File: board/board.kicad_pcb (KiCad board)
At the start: 2 copper layers, 45 x 94 mm, 13 parts, among them J1 020_1000BASE-T_with_CT, J2 003_power, J3 008_USB, J4 001_I2C, J5 008_USB, J6 002_SPI, J7 010_UART, U1 VAR-SOM

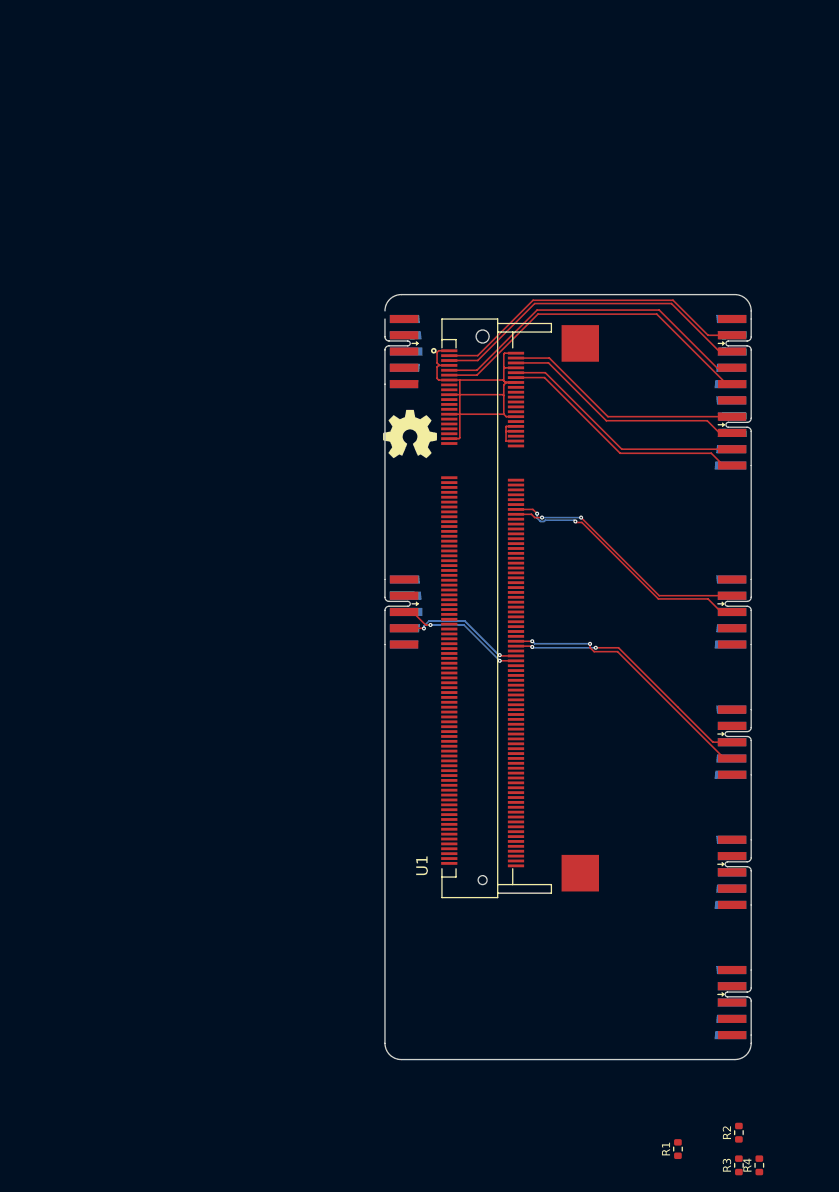
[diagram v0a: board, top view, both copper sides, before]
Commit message: added RGMII interface
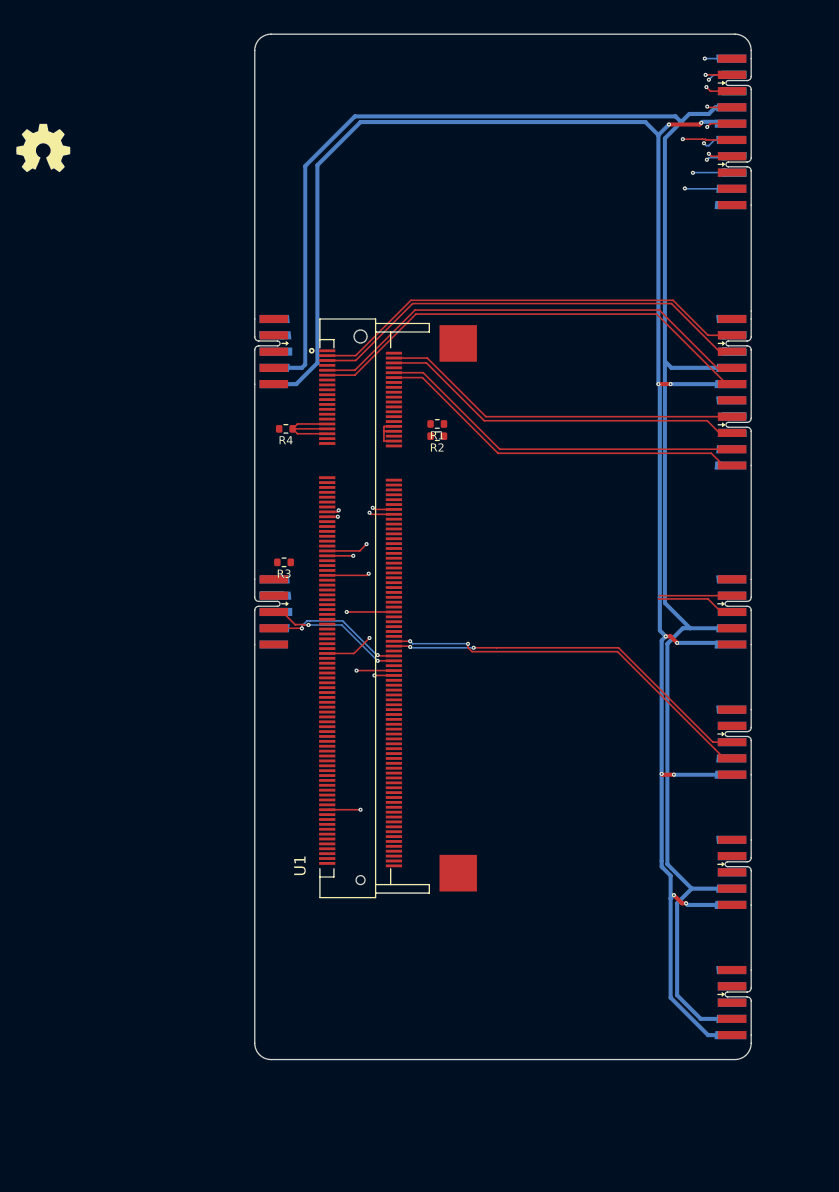
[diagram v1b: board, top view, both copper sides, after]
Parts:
- added J8: 015_RGMII, on_edge:on_edge_2x10_host, F.Cu at (174.0, 24.0)
- moved R4 107.6 mm to (116.8, 65.5), turned to 180 degrees
- moved R1 93.9 mm to (135.4, 64.9), turned to 180 degrees
- moved R2 93.3 mm to (135.4, 66.4), turned to 180 degrees
- moved R3 92.8 mm to (116.6, 81.9), turned to 180 degrees
- moved LOGO1 57.2 mm to (87.0, 31.0)
- moved J2 16.0 mm to (113.0, 56.0)
- moved J3 16.0 mm to (113.0, 88.0)
- moved U1 15.0 mm to (126.0, 87.5)
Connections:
- J1 pad 1: unconnected-(J1-Pad1) -> GND
- J1 pad 11: unconnected-(J1-Pad11) -> GND
- J3 pad 10: unconnected-(J3-Pad10) -> +5V
- J5 pad 10: unconnected-(J5-Pad10) -> +5V
- R1 pad 1: /var-som/VCC -> +3.3V
- R2 pad 1: /var-som/VCC -> +3.3V
- R3 pad 2: /var-som/VCC -> +3.3V
- R4 pad 2: /var-som/VCC -> +3.3V
- U1 pad 103: /var-som/VCC -> +3.3V
- U1 pad 105: /var-som/VCC -> +3.3V
- U1 pad 107: /var-som/VCC -> +3.3V
- U1 pad 109: /var-som/VCC -> +3.3V
- U1 pad 111: /var-som/VCC -> +3.3V
- U1 pad 113: unconnected-(U1-Pad113) -> /var-som/ENET1_TX_CTL
- U1 pad 120: unconnected-(U1-Pad120) -> /var-som/ENET1_RX_CTL
- U1 pad 122: unconnected-(U1-Pad122) -> /var-som/ENET1_RXD0
- U1 pad 177: unconnected-(U1-Pad177) -> /var-som/ENET1_TXD1
- U1 pad 32: /var-som/VCC -> +3.3V
- U1 pad 34: /var-som/VCC -> +3.3V
- U1 pad 38: /var-som/VCC -> +3.3V
- U1 pad 52: unconnected-(U1-Pad52) -> /UART5_TX
- U1 pad 53: unconnected-(U1-Pad53) -> /UART5_RX
- U1 pad 54: /UART5_RX -> /var-som/ENET1_RXD3
- U1 pad 55: unconnected-(U1-Pad55) -> /var-som/ENET1_TXD3
- U1 pad 56: /UART5_TX -> /var-som/ENET1_TXD2
- U1 pad 57: unconnected-(U1-Pad57) -> /var-som/ENET1_RXC
- U1 pad 71: unconnected-(U1-Pad71) -> /var-som/ENET1_RXD2
- U1 pad 73: unconnected-(U1-Pad73) -> /var-som/ENET1_TXD0
- U1 pad 81: unconnected-(U1-Pad81) -> /var-som/ENET1_RXD1
- U1 pad 96: unconnected-(U1-Pad96) -> /var-som/ENET1_TXC
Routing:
- net +5V: track 0.00 -> 235.5 mm, vias 0 -> 10
- net +3.3V: track 0.00 -> 229.3 mm
- net /var-som/ENET1_TXD1: track 0.00 -> 116.9 mm, vias 0 -> 2
- net /var-som/ENET1_RX_CTL: track 0.00 -> 104.3 mm, vias 0 -> 2
- net /var-som/ENET1_TXC: track 0.00 -> 98.3 mm, vias 0 -> 2
- net /var-som/ENET1_RXD0: track 0.00 -> 95.1 mm, vias 0 -> 2
- net /var-som/ENET1_TX_CTL: track 0.00 -> 92.2 mm, vias 0 -> 2
- net /var-som/ENET1_TXD0: track 0.00 -> 87.3 mm, vias 0 -> 2
- net /var-som/ENET1_RXC: track 0.00 -> 84.6 mm, vias 0 -> 2
- net /var-som/ENET1_RXD1: track 0.00 -> 82.9 mm, vias 0 -> 2
- net /var-som/ENET1_RXD2: track 0.00 -> 77.8 mm, vias 0 -> 2
- net /var-som/ENET1_TXD2: track 0.00 -> 76.9 mm, vias 0 -> 2
- net /var-som/ENET1_TXD3: track 0.00 -> 75.1 mm, vias 0 -> 2
- net /var-som/ENET1_RXD3: track 0.00 -> 68.9 mm, vias 0 -> 2
- net GND: track 51.3 -> 0.00 mm
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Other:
- board size 45 x 94 mm -> 61 x 126 mm
- copper layers 2 -> 4

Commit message: added uSD card
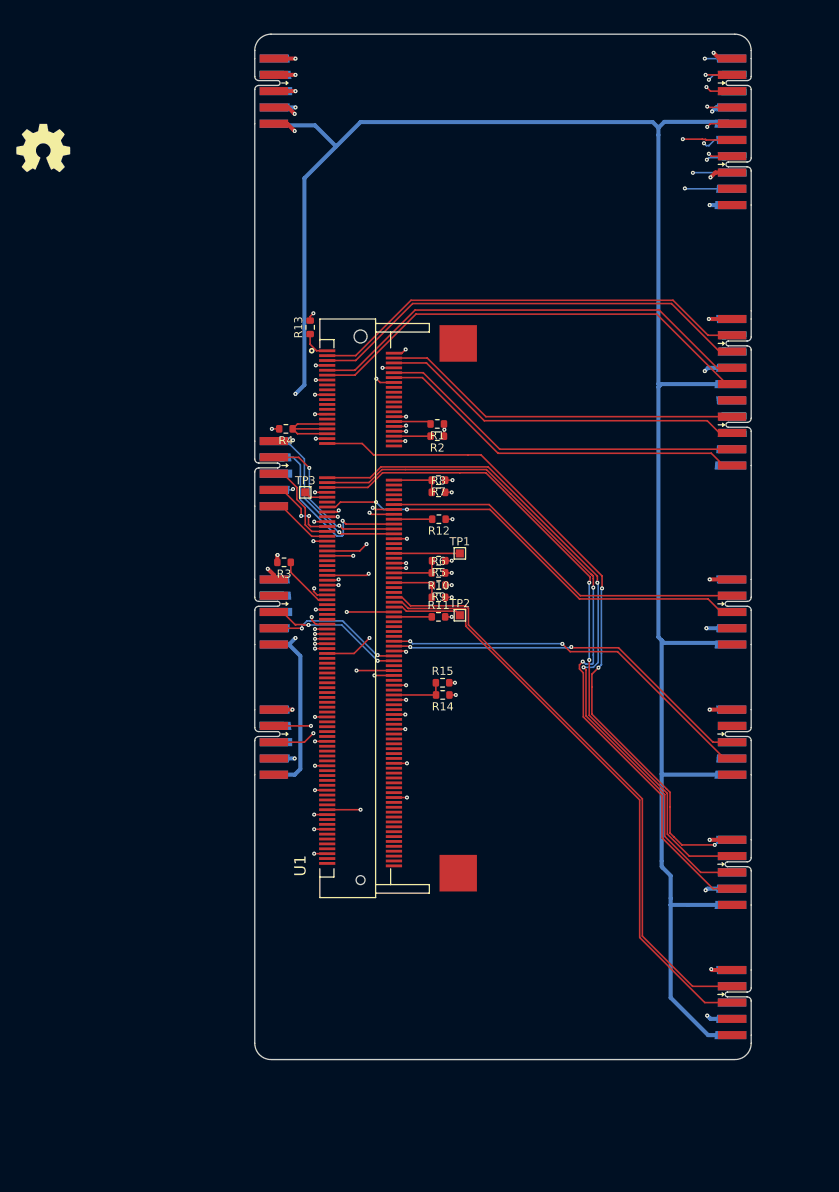
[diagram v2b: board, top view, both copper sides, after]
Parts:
- added J10: 018_QSPI, on_edge:on_edge_2x05_device, F.Cu at (113.0, 71.0)
- added J9: 010_UART, on_edge:on_edge_2x05_device, F.Cu at (113.0, 104.0)
- added R10: 560R, Resistor_SMD:R_0603_1608Metric, F.Cu at (135.6, 86.2)
- added R11: 560R, Resistor_SMD:R_0603_1608Metric, F.Cu at (135.6, 88.6)
- added R12: 0R, Resistor_SMD:R_0603_1608Metric, F.Cu at (135.6, 76.6)
- added R13: 0R, Resistor_SMD:R_0603_1608Metric, F.Cu at (119.8, 53.0)
- added R14: 0R, Resistor_SMD:R_0603_1608Metric, F.Cu at (136.1, 98.2)
- added R15: 560R, Resistor_SMD:R_0603_1608Metric, F.Cu at (136.1, 96.7)
- added R5: 560R, Resistor_SMD:R_0603_1608Metric, F.Cu at (135.6, 81.7)
- added R6: 560R, Resistor_SMD:R_0603_1608Metric, F.Cu at (135.6, 83.2)
- added R7: 560R, Resistor_SMD:R_0603_1608Metric, F.Cu at (135.6, 71.8)
- added R8: 560R, Resistor_SMD:R_0603_1608Metric, F.Cu at (135.6, 73.3)
- added R9: 0R, Resistor_SMD:R_0603_1608Metric, F.Cu at (135.6, 84.7)
- added TP1: USB_B_VBUS_ID1, TestPoint:TestPoint_Pad_1.0x1.0mm, F.Cu at (138.2, 80.8)
- added TP2: USB_B_VBUS_ID2, TestPoint:TestPoint_Pad_1.0x1.0mm, F.Cu at (138.2, 88.4)
- added TP3: base_peripherals_power, TestPoint:TestPoint_Pad_1.0x1.0mm, F.Cu at (119.2, 73.3)
- moved J2 32.0 mm to (113.0, 24.0)
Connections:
- J4 pad 2: unconnected-(J4-Pad2) -> /var-som/I2C3_SDA
- J4 pad 3: unconnected-(J4-Pad3) -> /var-som/I2C3_SCL
- J6 pad 2: unconnected-(J6-Pad2) -> /var-som/SPI4_MOSI
- J6 pad 3: unconnected-(J6-Pad3) -> /var-som/SPI4_MISO
- J6 pad 4: unconnected-(J6-Pad4) -> /var-som/SPI4_SCLK
- J6 pad 6: unconnected-(J6-Pad6) -> /var-som/SPI4_SS
- U1 pad 1: GND -> Net-(U1-Pad1)
- U1 pad 130: unconnected-(U1-Pad130) -> Net-(U1-Pad130)
- U1 pad 178: unconnected-(U1-Pad178) -> GND
- U1 pad 39: unconnected-(U1-Pad39) -> /var-som/SPI4_SS
- U1 pad 41: unconnected-(U1-Pad41) -> /var-som/SPI4_MISO
- U1 pad 42: unconnected-(U1-Pad42) -> /var-som/bootsel_a
- U1 pad 43: unconnected-(U1-Pad43) -> /var-som/SPI4_SCLK
- U1 pad 45: unconnected-(U1-Pad45) -> /var-som/SPI4_MOSI
- U1 pad 49: unconnected-(U1-Pad49) -> Net-(U1-Pad49)
- U1 pad 58: unconnected-(U1-Pad58) -> Net-(U1-Pad58)
- U1 pad 60: unconnected-(U1-Pad60) -> /var-som/uSDHC_CLK
- U1 pad 61: unconnected-(U1-Pad61) -> /var-som/uSDHC_D2
- U1 pad 62: unconnected-(U1-Pad62) -> /var-som/uSDHC_D0
- U1 pad 63: unconnected-(U1-Pad63) -> /var-som/uSDHC_D1
- U1 pad 64: unconnected-(U1-Pad64) -> /var-som/uSDHC_CMD
- U1 pad 65: unconnected-(U1-Pad65) -> /var-som/uSDHC_D3
- U1 pad 72: unconnected-(U1-Pad72) -> /var-som/USB_B_VBUS_ID1
- U1 pad 80: unconnected-(U1-Pad80) -> /var-som/bootsel_b
- U1 pad 83: unconnected-(U1-Pad83) -> /var-som/DEBUG_UART_RX
- U1 pad 84: unconnected-(U1-Pad84) -> Net-(U1-Pad84)
- U1 pad 85: unconnected-(U1-Pad85) -> /var-som/DEBUG_UART_TX
- U1 pad 90: unconnected-(U1-Pad90) -> /var-som/I2C3_SDA
- U1 pad 92: unconnected-(U1-Pad92) -> /var-som/I2C3_SCL
- U1 pad 94: unconnected-(U1-Pad94) -> /var-som/USB_B_VBUS_ID2
- U1 pad 98: unconnected-(U1-Pad98) -> Net-(U1-Pad98)
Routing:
- net +3.3V: track 229.3 -> 42.3 mm, vias 0 -> 24
- net GND: track 0.00 -> 100.7 mm, vias 0 -> 54
- net /var-som/SPI4_SCLK: track 0.00 -> 88.2 mm, vias 0 -> 2
- net /var-som/SPI4_MISO: track 0.00 -> 87.0 mm, vias 0 -> 2
- net /var-som/SPI4_SS: track 0.00 -> 85.0 mm, vias 0 -> 3
- net /var-som/SPI4_MOSI: track 0.00 -> 83.0 mm, vias 0 -> 2
- net /var-som/I2C3_SCL: track 0.00 -> 73.0 mm
- net /var-som/I2C3_SDA: track 0.00 -> 72.4 mm
- net +5V: track 235.5 -> 295.7 mm, vias 10 -> 2
- net /UART5_RX: track 9.71 -> 55.6 mm, vias 0 -> 2
- net /UART5_TX: track 8.95 -> 46.2 mm
- net /var-som/DEBUG_UART_TX: track 0.00 -> 26.2 mm, vias 0 -> 2
- net /var-som/DEBUG_UART_RX: track 0.00 -> 25.8 mm, vias 0 -> 2
- net /var-som/uSDHC_CLK: track 0.00 -> 23.6 mm, vias 0 -> 1
- net /var-som/uSDHC_CMD: track 0.00 -> 22.2 mm, vias 0 -> 1
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- added copper zone on In1.Cu, net +3.3V
- added copper zone on In2.Cu, net GND
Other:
- outline, holes or cut-outs redrawn

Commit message: added 1.8v power option for RGMII IO
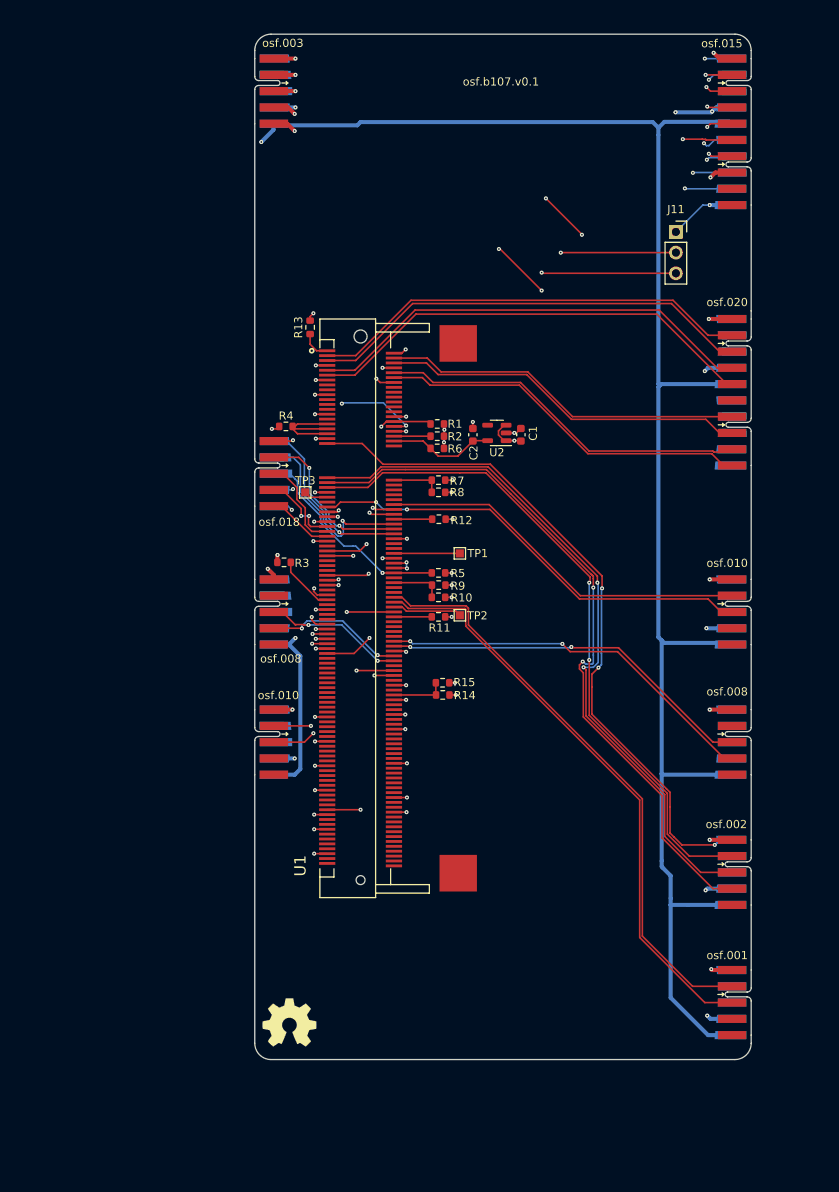
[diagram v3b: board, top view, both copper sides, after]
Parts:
- added C1: 4.7uF, Capacitor_SMD:C_0603_1608Metric, F.Cu at (145.7, 66.2)
- added C2: 4.7uF, Capacitor_SMD:C_0603_1608Metric, F.Cu at (139.8, 66.2)
- added J11: Conn_01x03_Male, Connector_PinSocket_2.54mm:PinSocket_1x03_P2.54mm_Vertical, F.Cu at (164.8, 41.3)
- added U2: TLV71318PQDBVRQ1, Package_TO_SOT_SMD:SOT-23-5, F.Cu at (142.8, 66.0)
- R5: value 560R -> 10k
- R6: value 560R -> 0R
- moved LOGO1 111.6 mm to (117.2, 138.4)
- moved R6 15.3 mm to (135.4, 67.9), turned to 180 degrees
- moved R5 1.50 mm to (135.6, 83.2), turned to 0 degrees
- moved R4 0.30 mm to (116.8, 65.2)
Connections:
- net Net-(R1-Pad2) renamed /var-som/MDIO
- J10 pad 10: (no net) -> GND
- J10 pad 8: (no net) -> /var-som/bootsel_b
- R5 pad 1: GND -> /var-som/bootsel_b
- R5 pad 2: /var-som/bootsel_b -> +3.3V
- R6 pad 1: /var-som/bootsel_b -> +3.3V
- R6 pad 2: +3.3V -> /var-som/ETH1_VDDIO
- U1 pad 38: +3.3V -> /var-som/ETH1_VDDIO
- U1 pad 74: unconnected-(U1-Pad74) -> /var-som/MDC
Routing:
- net +3.3V: track 42.3 -> 117.0 mm, vias 24 -> 31
- net /var-som/MDC: track 0.00 -> 61.4 mm, vias 0 -> 2
- net /var-som/MDIO: track 4.62 -> 51.6 mm, vias 0 -> 2
- net /var-som/bootsel_b: track 6.16 -> 25.5 mm, vias 0 -> 1
- net /var-som/ETH1_VDDIO: track 0.00 -> 13.1 mm
- net GND: track 100.7 -> 113.2 mm, vias 54 -> 57
- net +5V: track 295.7 -> 298.0 mm
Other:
- board text added: "osf.001"
- board text added: "osf.002"
- board text added: "osf.003"
- board text added: "osf.008"
- board text added: "osf.010"
- board text added: "osf.015"
- board text added: "osf.018"
- board text added: "osf.020"
- board text added: "osf.b107.v0.1"

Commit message: increased spacing
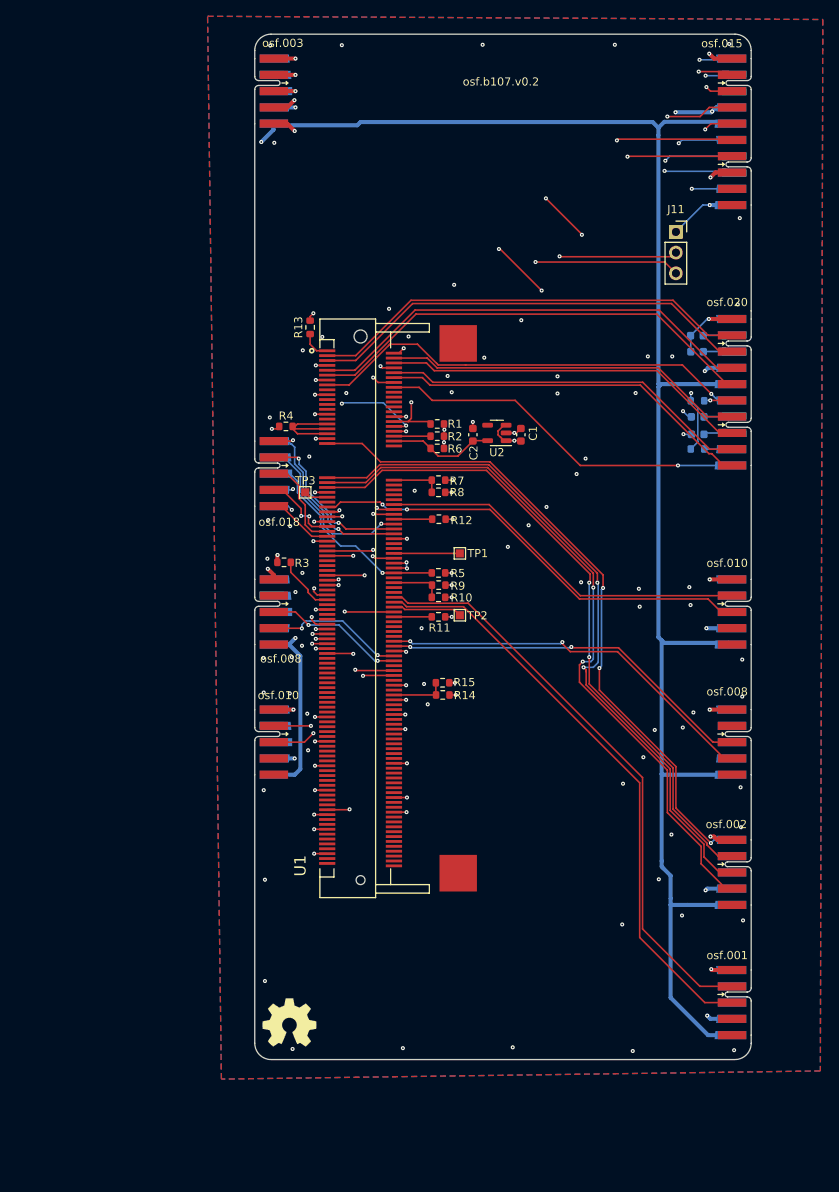
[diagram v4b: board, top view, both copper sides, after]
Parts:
- added C3: 100nF, Capacitor_SMD:C_0603_1608Metric, B.Cu at (167.3, 54.0)
- added C4: 100nF, Capacitor_SMD:C_0603_1608Metric, B.Cu at (167.3, 56.0)
- added C5: 100nF, Capacitor_SMD:C_0603_1608Metric, B.Cu at (167.4, 64.0)
- added C6: 100nF, Capacitor_SMD:C_0603_1608Metric, B.Cu at (167.4, 66.2)
- added R16: 49.9R, Resistor_SMD:R_0603_1608Metric, B.Cu at (167.4, 62.0)
- added R17: 49.9R, Resistor_SMD:R_0603_1608Metric, B.Cu at (167.4, 68.0)
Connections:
- J1 pad 12: unconnected-(J1-Pad12) -> Net-(J1-Pad12)
- J1 pad 13: unconnected-(J1-Pad13) -> Net-(J1-Pad13)
- J1 pad 16: unconnected-(J1-Pad16) -> /led1
- J1 pad 17: unconnected-(J1-Pad17) -> Net-(J1-Pad17)
- J1 pad 18: unconnected-(J1-Pad18) -> Net-(J1-Pad18)
- J1 pad 19: unconnected-(J1-Pad19) -> Net-(J1-Pad19)
- J1 pad 20: unconnected-(J1-Pad20) -> /led2
- J1 pad 6: unconnected-(J1-Pad6) -> Net-(J1-Pad6)
- U1 pad 15: /var-som/ETH_A_LED_ACT -> /led1
- U1 pad 16: /var-som/ETH_A_LED_SPD -> /led2
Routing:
- net /led1: track 0.00 -> 54.6 mm, vias 0 -> 1
- net /led2: track 0.00 -> 45.4 mm, vias 0 -> 1
- net +3.3V: track 117.0 -> 128.1 mm, vias 31 -> 32
- net GND: track 113.2 -> 121.9 mm, vias 57 -> 132
- net /var-som/ENET1_RXC: track 84.6 -> 80.2 mm
- net /var-som/MDC: track 61.4 -> 65.7 mm
- net /var-som/MDIO: track 51.6 -> 47.5 mm
- net Net-(J1-Pad12): track 0.00 -> 3.82 mm
- net Net-(J1-Pad13): track 0.00 -> 3.79 mm
- net Net-(J1-Pad18): track 0.00 -> 3.77 mm
- net /var-som/ENET1_RX_CTL: track 104.3 -> 100.5 mm
- net /var-som/ENET1_TXD0: track 87.3 -> 83.5 mm
- net Net-(J1-Pad17): track 0.00 -> 3.71 mm
- net Net-(J1-Pad6): track 0.00 -> 3.45 mm, vias 0 -> 1
- net /var-som/ENET1_TXD1: track 116.9 -> 113.5 mm
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- added copper zone on B.Cu, net GND
- added copper zone on F.Cu, net GND
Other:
- board text added: "osf.b107.v0.2"
- board text removed: "osf.b107.v0.1"
